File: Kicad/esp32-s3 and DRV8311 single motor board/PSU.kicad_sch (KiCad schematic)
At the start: 29 parts, among them Q1 NMOS, sir404dp, Q2 NMOS, Q3 PMOS,Si7157DP, Q4 PMOS, U3 BQ298012RUGT, U4 BQ25060

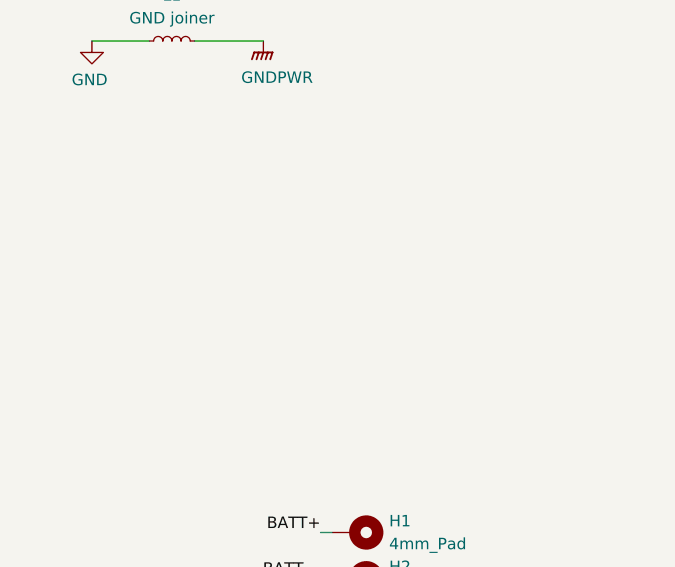
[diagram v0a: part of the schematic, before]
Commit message: Mostly finished draft wiring
I added test points to practically every pin I won't be using regularly. Even if I never use a pin, it is better to have it exposed somehow than to try to solder to a tiny pitch pad
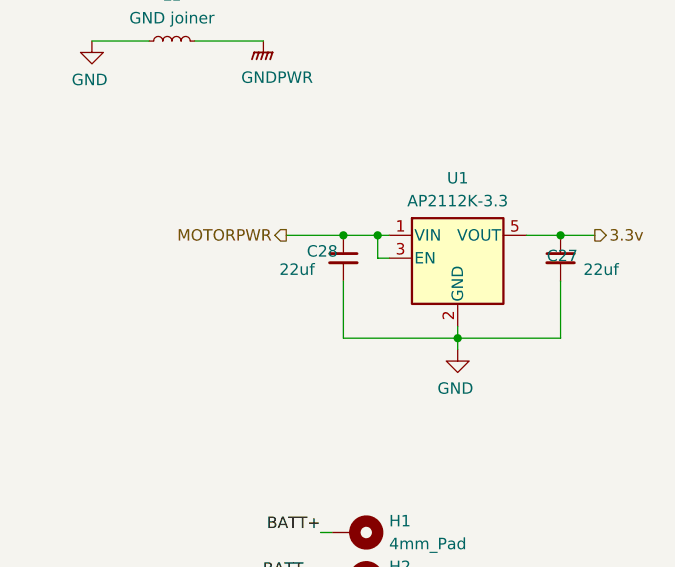
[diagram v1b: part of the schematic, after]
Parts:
- added C27, C28: 22uf, Capacitor_SMD:C_0603_1608Metric, symbol Device:C_Small
- added U1: AP2112K-3.3, Package_TO_SOT_SMD:SOT-23-5, symbol Regulator_Linear:AP2112K-3.3
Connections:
- net GND: now also C27.2, C28.2, U1.2 (GND)
- net MOTORPWR: now also C28.1, U1.1 (VIN), U1.3 (EN)
- new net 3.3v: C27.1, U1.5 (VOUT)

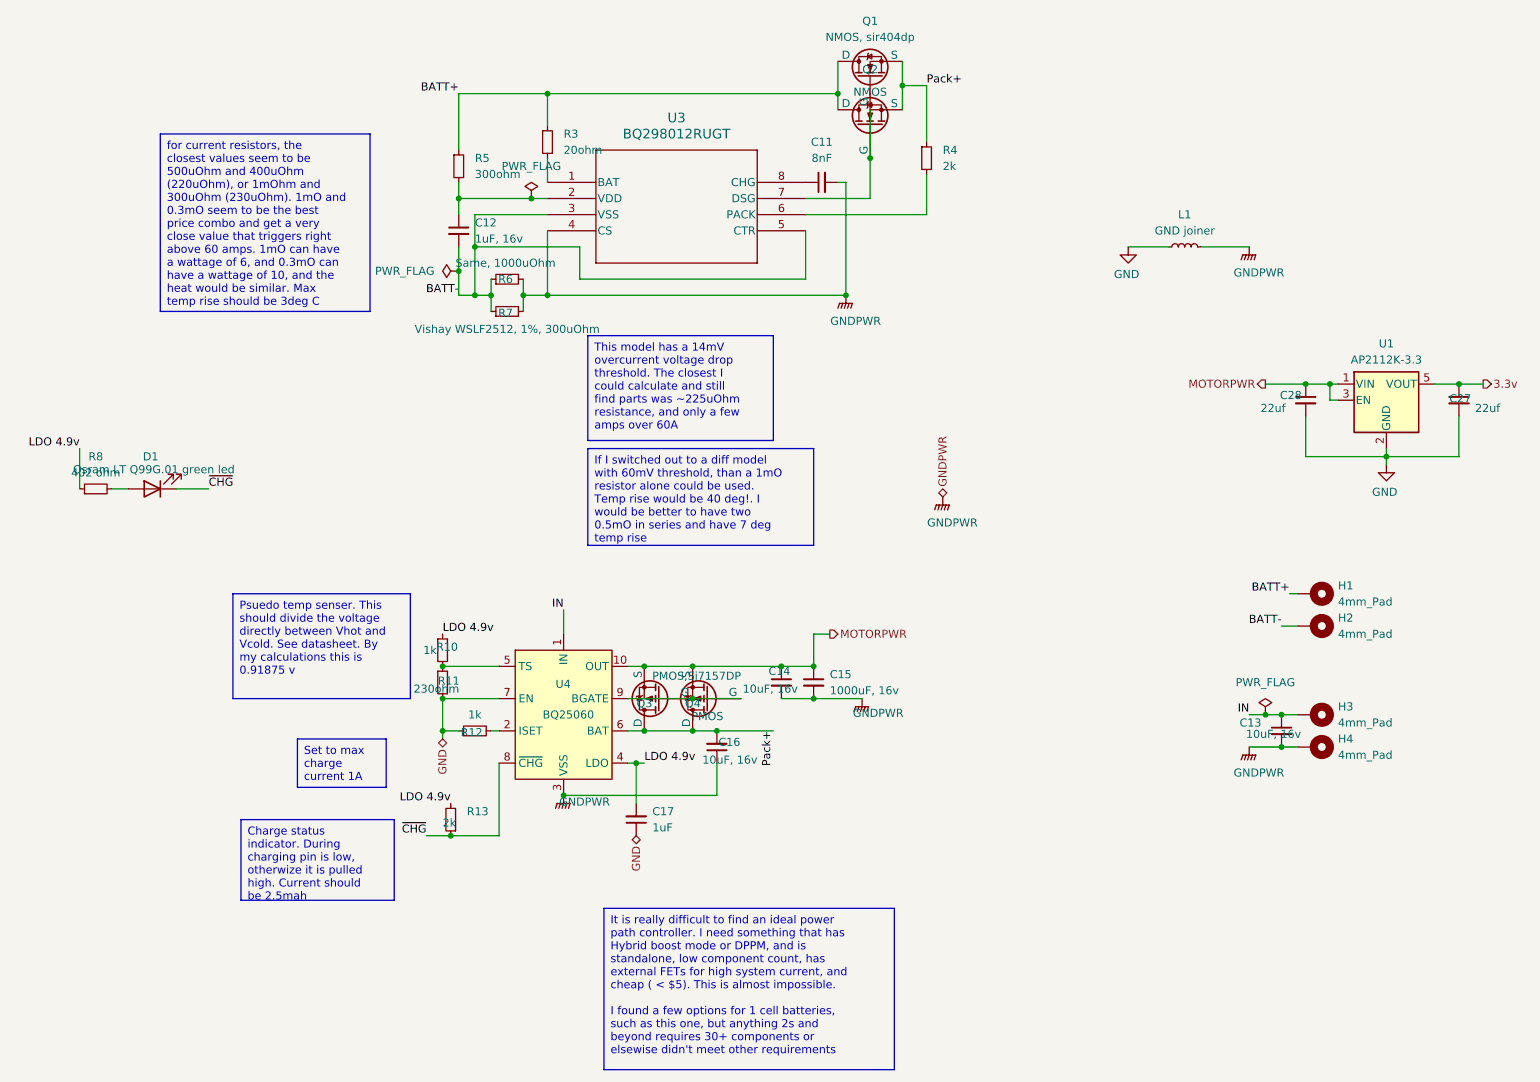
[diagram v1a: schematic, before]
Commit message: Finished schematic and fixed DRC errors
Now I'm moving on to layout.
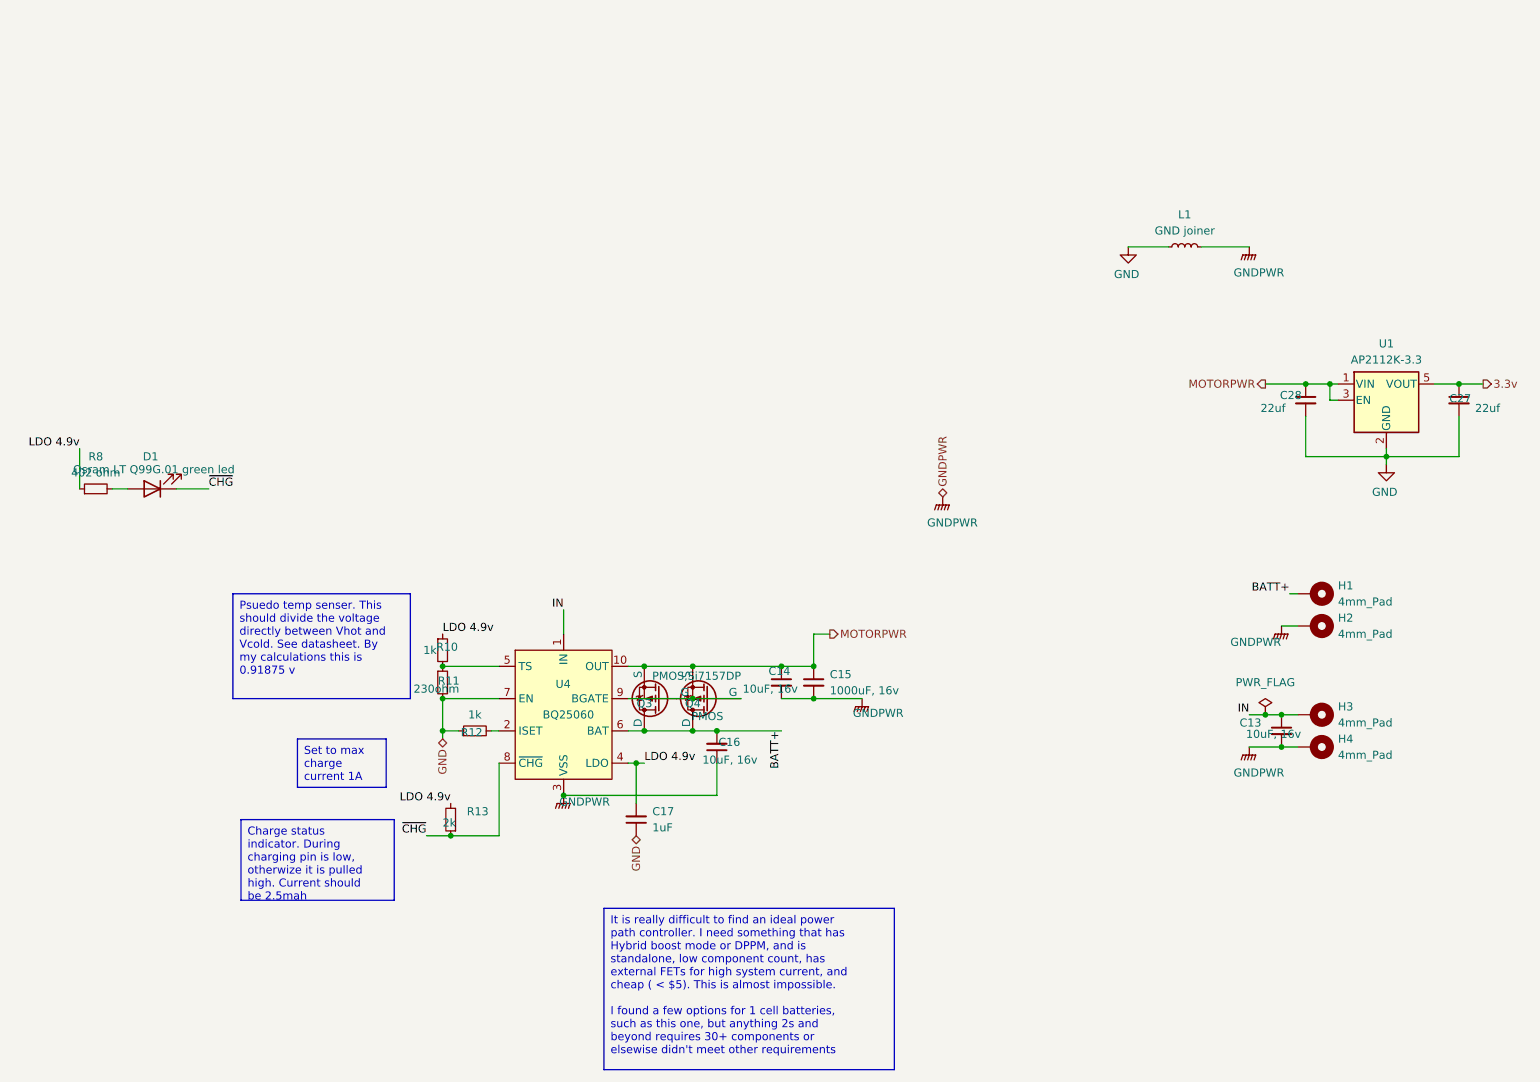
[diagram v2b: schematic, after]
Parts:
- removed C11: 8nF, Capacitor_SMD:C_0603_1608Metric, symbol Device:C_Small
- removed C12: 1uF, 16v, Capacitor_SMD:C_0603_1608Metric, symbol Device:C_Small
- removed Q1: NMOS, sir404dp, Package_DFN_QFN:PQFN-8-EP_6x5mm_P1.27mm_Generic, symbol Simulation_SPICE:NMOS
- removed Q2: NMOS, Package_DFN_QFN:PQFN-8-EP_6x5mm_P1.27mm_Generic, symbol Simulation_SPICE:NMOS
- removed R3: 20ohm, Resistor_SMD:R_0603_1608Metric, symbol Device:R_Small
- removed R4: 2k, Resistor_SMD:R_0603_1608Metric_Pad0.98x0.95mm_HandSolder, symbol Device:R_Small
- removed R5: 300ohm, Resistor_SMD:R_0603_1608Metric, symbol Device:R_Small
- removed R6: Same, 1000uOhm, vishay_wslf:RES_WSLF2512_VIS-M, symbol Device:R_Small
- removed R7: Vishay WSLF2512, 1%, 300uOhm, vishay_wslf:RES_WSLF2512_VIS-M, symbol Device:R_Small
- removed U3: BQ298012RUGT, bq298rugt:RUG8_TEX, symbol bq298xyz:BQ298000RUGT
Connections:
- net BATT- is gone; now on net GNDPWR: H2.1
- net Pack+ is gone; now on net BATT+: C16.2, Q3.5 (D), Q4.5 (D), U4.6 (BAT)

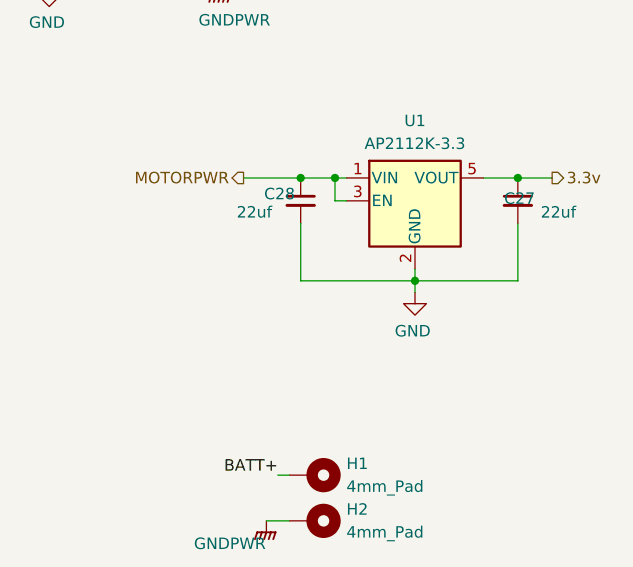
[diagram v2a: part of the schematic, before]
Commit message: Routing test pads & power
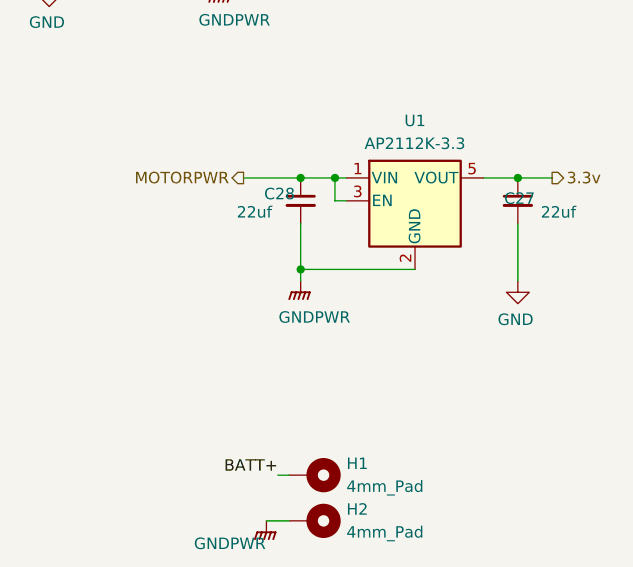
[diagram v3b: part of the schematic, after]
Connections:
- net GND: no longer C28.2, U1.2 (GND)
- net GNDPWR: now also C28.2, U1.2 (GND)
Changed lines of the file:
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@@
-	)
-	(junction
-		(at 233.68 87.63)
-		(diameter 0)
-		(color 0 0 0 0)
 	)
 	(junction
@@
 	)
 	(junction
+		(at 220.98 86.36)
+		(diameter 0)
+		(color 0 0 0 0)
+	)
+	(junction
 		(at 128.27 130.81)
 		(diameter 0)
@@
 	(wire
 		(pts
-			(xy 233.68 87.63) (xy 233.68 86.36)
+			(xy 233.68 86.36) (xy 220.98 86.36)
 		)
 		(stroke
@@
 	(wire
 		(pts
-			(xy 220.98 81.28) (xy 220.98 87.63)
+			(xy 220.98 81.28) (xy 220.98 86.36)
 		)
 		(stroke
@@
 	(wire
 		(pts
+			(xy 220.98 86.36) (xy 220.98 87.63)
+		)
+		(stroke
+			(width 0)
+			(type default)
+		)
+	)
+	(wire
+		(pts
 			(xy 217.17 128.27) (xy 219.71 128.27)
 		)
@@
 	(wire
 		(pts
-			(xy 245.11 87.63) (xy 233.68 87.63)
-		)
-		(stroke
-			(width 0)
-			(type default)
-		)
-	)
-	(wire
-		(pts
 			(xy 93.98 147.32) (xy 93.98 135.89)
 		)
@@
 	(wire
 		(pts
-			(xy 233.68 88.9) (xy 233.68 87.63)
-		)
-		(stroke
-			(width 0)
-			(type default)
-		)
-	)
-	(wire
-		(pts
 			(xy 85.09 130.81) (xy 87.63 130.81)
 		)
@@
 		(pts
 			(xy 217.17 114.3) (xy 219.71 114.3)
-		)
-		(stroke
-			(width 0)
-			(type default)
-		)
-	)
-	(wire
-		(pts
-			(xy 220.98 87.63) (xy 233.68 87.63)
 		)
 		(stroke
@@
 	(symbol
 		(lib_id "power:GND")
-		(at 233.68 88.9 0)
+		(at 245.11 87.63 0)
 		(unit 1)
 		(exclude_from_sim no)
@@
 		(dnp no)
 		(property "Reference" "#PWR05"
-			(at 233.68 95.25 0)
+			(at 245.11 93.98 0)
 			(effects
 				(font
@@
 		)
 		(property "Value" "GND"
-			(at 233.426 93.218 0)
+			(at 244.856 91.948 0)
 			(effects
 				(font
@@
 		)
 		(property "Footprint" ""
-			(at 233.68 88.9 0)
+			(at 245.11 87.63 0)
 			(effects
 				(font
@@
 		)
 		(property "Datasheet" ""
-			(at 233.68 88.9 0)
+			(at 245.11 87.63 0)
 			(effects
 				(font
@@
 		)
 		(property "Description" "Power symbol creates a global label with name \"GND\" , ground"
-			(at 233.68 88.9 0)
+			(at 245.11 87.63 0)
 			(effects
 				(font
@@
 					(unit 1)
 				)
+			)
+		)
+	)
+	(symbol
+		(lib_id "power:GNDPWR")
+		(at 220.98 87.63 0)
+		(unit 1)
+		(exclude_from_sim no)
+		(in_bom yes)
+		(on_board yes)
+		(dnp no)
+		(property "Reference" "#PWR038"
+			(at 220.98 92.71 0)
+			(effects
+				(font
+					(size 1.27 1.27)
+				)
+				(hide yes)
+			)
+		)
+		(property "Value" "GNDPWR"
+			(at 222.504 91.694 0)
+			(effects
+				(font
+					(size 1.27 1.27)
+				)
+			)
+		)
+		(property "Footprint" ""
+			(at 220.98 88.9 0)
+			(effects
+				(font
+					(size 1.27 1.27)
+				)
+				(hide yes)
+			)
+		)
+		(property "Datasheet" ""
+			(at 220.98 88.9 0)
+			(effects
+				(font
+					(size 1.27 1.27)
+				)
+				(hide yes)
+			)
+		)
+		(property "Description" "Power symbol creates a global label with name \"GNDPWR\" , global ground"
+			(at 220.98 87.63 0)
+			(effects
+				(font
+					(size 1.27 1.27)
+				)
+				(hide yes)
+			)
+		)
+		(pin "1"
+		)
+		(instances
+			(project "esp32-s3 and DRV8311 single motor board"
+				(path "/eb3f183d-8bb1-43a5-a363-092ed67891e3/a57a0b4f-e246-497c-8d94-688647d8fd03"
+					(reference "#PWR038")
+					(unit 1)
+				)
